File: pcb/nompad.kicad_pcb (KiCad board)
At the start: 2 copper layers, 80.6 x 103.9 mm, 44 parts, among them J1 Conn_01x02_Pin, SW1 ChocHS, SW10 ChocHS, SW11 ChocHS, SW12 ChocHS, SW13 ChocHS, SW14 ChocHS, SW15 ChocHS, SW16 ChocHS, SW17 ChocHS, SW18 ChocHS, SW2 ChocHS, SW3 ChocHS, SW4 ChocHS, SW5 ChocHS, SW6 ChocHS, SW7 ChocHS, SW8 ChocHS, SW9 ChocHS

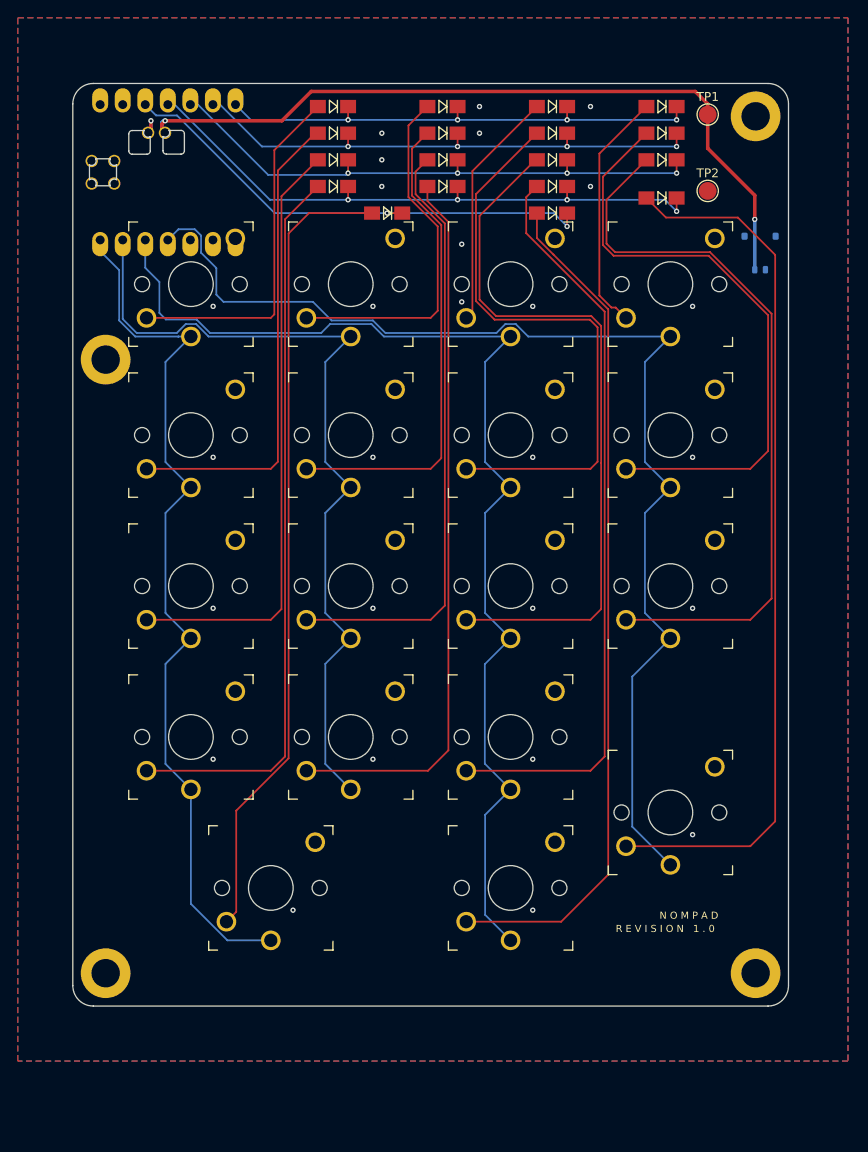
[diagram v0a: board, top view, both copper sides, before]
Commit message: Move one of the screw sockets under case
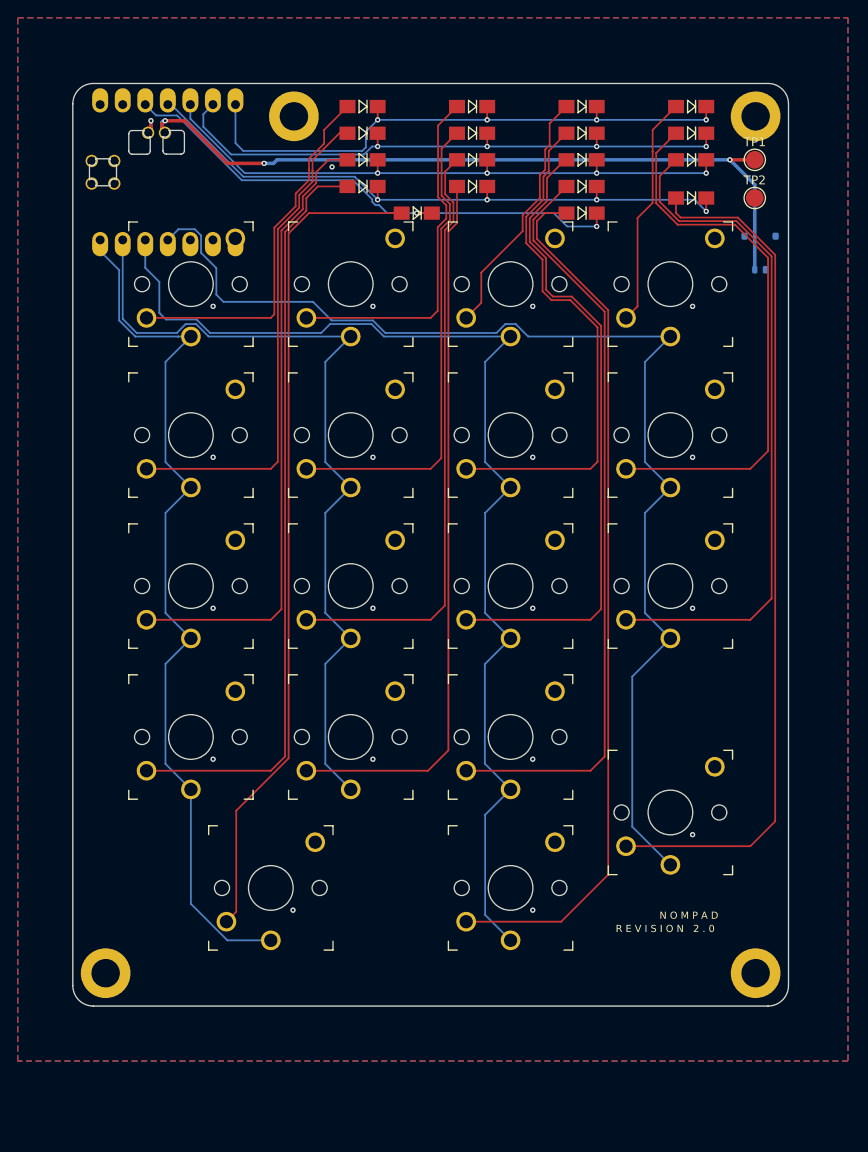
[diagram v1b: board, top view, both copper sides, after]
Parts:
- moved REF** 34.6 mm to (132.6, 49.1)
- moved TP1 7.36 mm to (184.5, 54.0)
- moved TP2 5.36 mm to (184.5, 58.3)
- moved D1 3.33 mm to (140.3, 48.0)
- moved D11 3.33 mm to (165.0, 54.0)
- moved D12 3.33 mm to (177.3, 54.0)
- moved D13 3.33 mm to (140.3, 57.0)
- moved D15 3.33 mm to (165.0, 57.0)
- moved D16 3.33 mm to (177.3, 58.3)
- moved D17 3.33 mm to (146.4, 60.0)
- moved D18 3.33 mm to (165.0, 60.0)
- moved D3 3.33 mm to (165.0, 48.0)
- moved D4 3.33 mm to (177.3, 48.0)
- moved D5 3.33 mm to (140.3, 51.0)
- moved D7 3.33 mm to (165.0, 51.0)
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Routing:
- net /ROW0: track 56.4 -> 66.2 mm
- net Net-(D11-A): track 81.1 -> 72.7 mm
- net Net-(D7-A): track 66.9 -> 58.6 mm
- net /ROW1: track 60.2 -> 68.1 mm
- net Net-(D12-A): track 82.6 -> 76.6 mm
- net Net-(D8-A): track 68.6 -> 62.5 mm
- net /ROW2: track 64.2 -> 68.3 mm
- net /ROW4: track 56.4 -> 59.8 mm
- net /ROW3: track 68.3 -> 71.7 mm
- net Net-(D17-A): track 90.8 -> 94.1 mm
- net Net-(D13-A): track 82.0 -> 85.3 mm
- net Net-(D18-A): track 96.0 -> 98.8 mm
- net Net-(D9-A): track 68.0 -> 70.6 mm
- net Net-(D16-A): track 98.9 -> 96.6 mm
- net BAT: track 86.5 -> 84.6 mm, vias 2 -> 3
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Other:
- board text added: "R E V I S I O N 2 . 0"
- board text removed: "R E V I S I O N 1 . 0"

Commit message: Cleanup
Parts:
- moved TP2 1.84 mm to (185.7, 59.7)
- moved TP1 1.84 mm to (185.7, 55.4)
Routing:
- net /ROW0: track 66.2 -> 68.0 mm
- net BAT: track 84.6 -> 86.4 mm
- net Net-(D11-A): track 72.7 -> 73.4 mm
- net Net-(D15-A): track 85.3 -> 86.0 mm

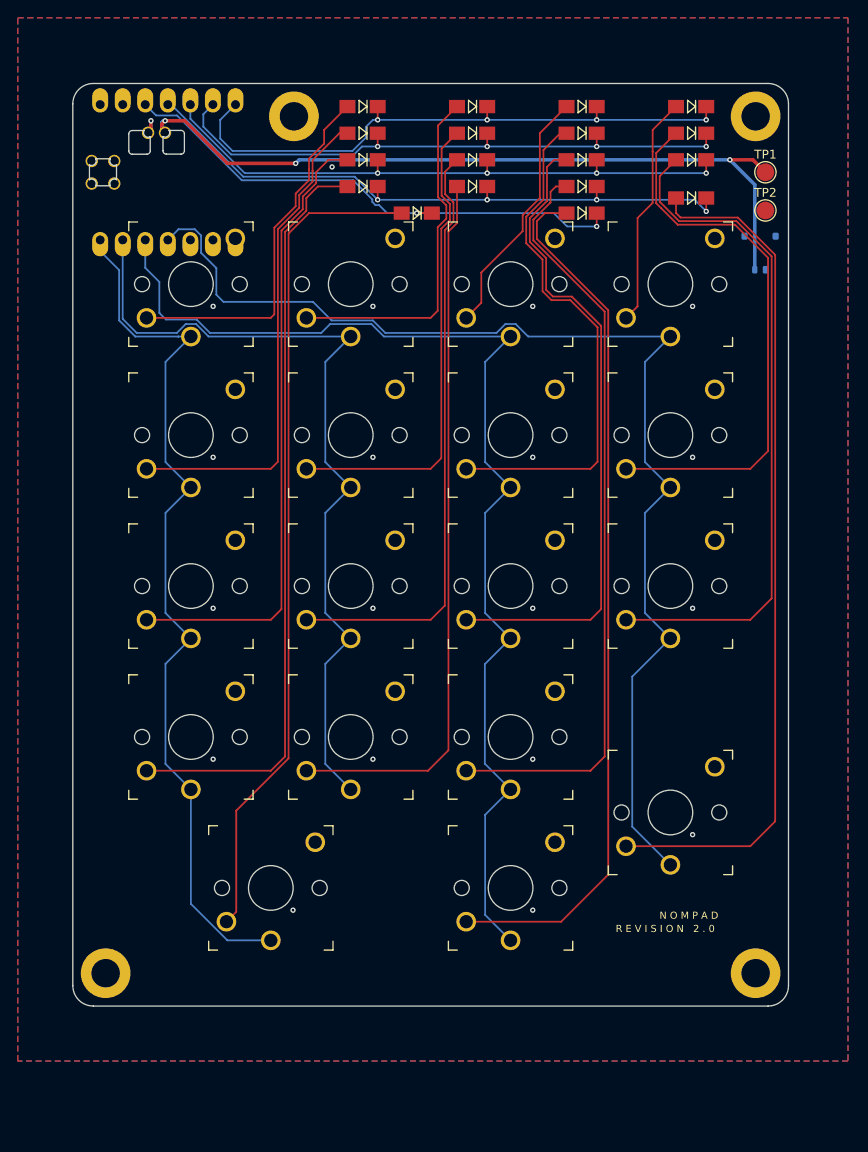
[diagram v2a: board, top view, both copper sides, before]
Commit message: Center everything
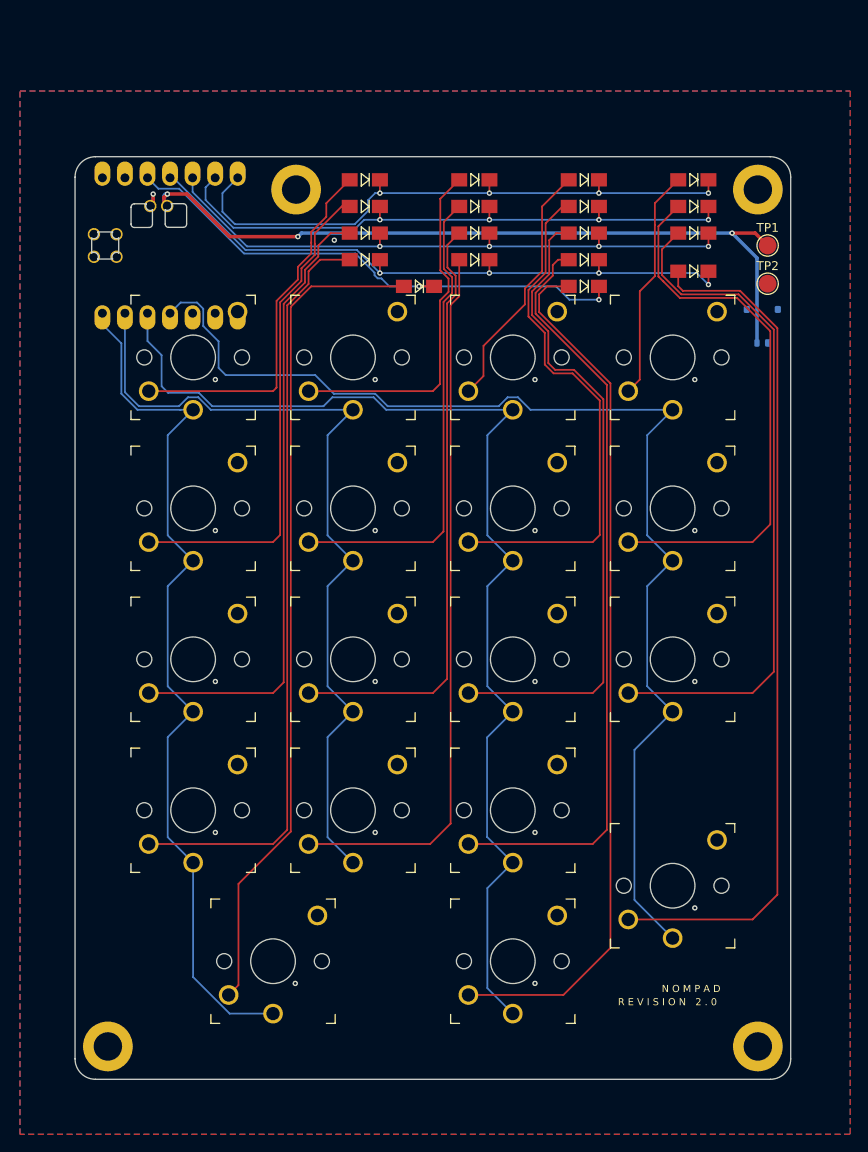
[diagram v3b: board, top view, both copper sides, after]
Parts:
- moved D1 8.25 mm to (140.6, 56.2)
- moved D10 8.25 mm to (152.9, 62.2)
- moved D11 8.25 mm to (165.2, 62.2)
- moved D12 8.25 mm to (177.6, 62.2)
- moved D13 8.25 mm to (140.6, 65.2)
- moved D14 8.25 mm to (152.9, 65.2)
- moved D15 8.25 mm to (165.2, 65.2)
- moved D16 8.25 mm to (177.6, 66.5)
- moved D17 8.25 mm to (146.7, 68.2)
- moved D18 8.25 mm to (165.2, 68.2)
- moved D2 8.25 mm to (152.9, 56.2)
- moved D3 8.25 mm to (165.2, 56.2)
- moved D4 8.25 mm to (177.6, 56.2)
- moved D5 8.25 mm to (140.6, 59.2)
- moved D6 8.25 mm to (152.9, 59.2)
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
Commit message: Align socket
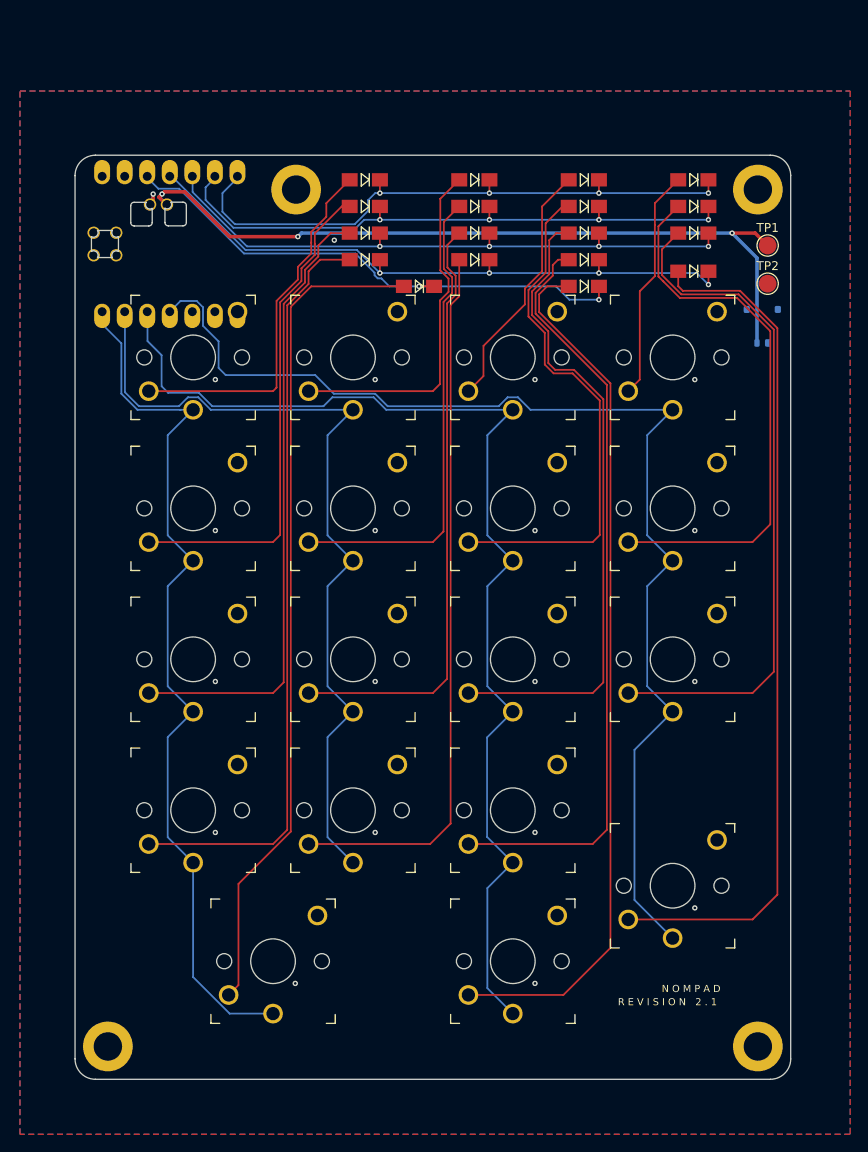
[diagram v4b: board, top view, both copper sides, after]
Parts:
- moved LU1 0.17 mm to (118.6, 63.5)
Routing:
- net BAT: track 86.4 -> 87.2 mm
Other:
- board size 80.6 x 103.9 mm -> 80.6 x 104.1 mm
- board text added: "R E V I S I O N 2 . 1"
- board text removed: "R E V I S I O N 2 . 0"
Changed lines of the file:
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@@
 		(title "Nompad")
 		(date "2025-05-27")
-		(rev "2.0")
+		(rev "2.1")
 	)
 	(layers
@@
 	(footprint "pcb-footprints:xiao-ble-smd-cutout-aternate"
 		(layer "B.Cu")
-		(at 118.65 63.65 -90)
+		(at 118.62 63.48 -90)
 		(property "Reference" "LU1"
 			(at -19.3989 11.28268 90)
@@
 	)
 	(gr_line
-		(start 188.55 55.95)
+		(start 188.55 55.78)
 		(end 188.55 155.25)
 		(stroke
@@
 	)
 	(gr_line
-		(start 107.95 55.95)
+		(start 107.95 55.78)
 		(end 107.95 155.25)
 		(stroke
@@
 	)
 	(gr_arc
-		(start 186.25 53.65)
-		(mid 187.876346 54.323654)
-		(end 188.55 55.95)
+		(start 186.25 53.48)
+		(mid 187.876346 54.153654)
+		(end 188.55 55.78)
 		(stroke
 			(width 0.1)
@@
 	)
 	(gr_line
-		(start 186.25 53.65)
-		(end 110.25 53.65)
+		(start 186.25 53.48)
+		(end 110.25 53.48)
 		(stroke
 			(width 0.1)
@@
 	)
 	(gr_arc
-		(start 107.95 55.95)
-		(mid 108.623654 54.323654)
-		(end 110.25 53.65)
+		(start 107.95 55.78)
+		(mid 108.623654 54.153654)
+		(end 110.25 53.48)
 		(stroke
 			(width 0.1)
@@
 		)
 	)
-	(gr_text "R E V I S I O N   2 . 0"
+	(gr_text "R E V I S I O N   2 . 1"
 		(at 169.083809 148.84 0)
 		(layer "F.SilkS")
@@
 	)
 	(segment
-		(start 181.95 62.25)
-		(end 184.55 62.25)
+		(start 118 57.6)
+		(end 117.75 57.85)
+		(width 0.4)
+		(layer "F.Cu")
+		(net 2)
+	)
+	(segment
+		(start 117.4 58.2)
+		(end 117.949481 58.749481)
 		(width 0.4)
 		(layer "F.Cu")
@@
 	)
 	(segment
-		(start 118.35 57.85)
-		(end 117.971061 58.228939)
+		(start 125.35 62.65)
+		(end 120.3 57.6)
 		(width 0.4)
 		(layer "F.Cu")
@@
 	)
 	(segment
-		(start 117.971061 58.228939)
-		(end 117.971061 58.922401)
+		(start 181.95 62.25)
+		(end 184.55 62.25)
 		(width 0.4)
 		(layer "F.Cu")
@@
 	)
 	(segment
-		(start 120.55 57.85)
-		(end 118.35 57.85)
+		(start 120.3 57.6)
+		(end 118 57.6)
 		(width 0.4)
 		(layer "F.Cu")
@@
 	)
 	(segment
-		(start 125.35 62.65)
-		(end 120.55 57.85)
+		(start 117.75 57.85)
+		(end 117.4 58.2)
 		(width 0.4)
 		(layer "F.Cu")
@@
 	)
 	(via
-		(at 181.95 62.25)
+		(at 117.75 57.85)
 		(size 0.6)
 		(drill 0.3)
@@
 	)
 	(via
-		(at 118.35 57.85)
+		(at 181.95 62.25)
 		(size 0.6)
 		(drill 0.3)
 		(layers "F.Cu" "B.Cu")
-		(free yes)
 		(net 2)
 	)
 	(segment
-		(start 118.009182 58.509182)
-		(end 118.009182 58.909182)
+		(start 117.4 58.2)
+		(end 117.949481 58.749481)
 		(width 0.4)
 		(layer "B.Cu")
@@
 	)
 	(segment
-		(start 118.35 57.85)
-		(end 118.15 57.85)
+		(start 117.75 57.85)
+		(end 117.4 58.2)
 		(width 0.4)
 		(layer "B.Cu")
@@
 	)
 	(segment
-		(start 118.15 57.85)
-		(end 118.009182 57.990818)
-		(width 0.4)
-		(layer "B.Cu")
-		(net 2)
-	)
-	(segment
-		(start 118.009182 57.990818)
-		(end 118.009182 58.509182)
-		(width 0.4)
-		(layer "B.Cu")
-		(net 2)
-	)
-	(segment
 		(start 133.45 62.25)
 		(end 181.95 62.25)
@@
 	)
 	(segment
-		(start 119.851 70.069)
-		(end 118.65 71.27)
-		(width 0.2)
-		(layer "B.Cu")
-		(net 14)
-	)
-	(segment
 		(start 159.239799 82.15)
 		(end 157.832799 80.743)
@@
 	)
 	(segment
-		(start 122.391 72.71747)
-		(end 122.391 70.77253)
-		(width 0.2)
-		(layer "B.Cu")
-		(net 14)
-	)
-	(segment
 		(start 143.157301 81.749)
 		(end 141.750301 80.342)
@@
 	)
 	(segment
-		(start 124.1155 74.44197)
-		(end 122.391 72.71747)
-		(width 0.2)
-		(layer "B.Cu")
-		(net 14)
-	)
-	(segment
-		(start 122.391 70.77253)
-		(end 121.68747 70.069)
+		(start 122.361 72.68747)
+		(end 122.361 70.60253)
 		(width 0.2)
 		(layer "B.Cu")
@@
 	)
 	(segment
-		(start 121.68747 70.069)
-		(end 119.851 70.069)
+		(start 119.821 69.899)
+		(end 118.62 71.1)
+		(width 0.2)
+		(layer "B.Cu")
+		(net 14)
+	)
+	(segment
+		(start 124.1155 74.44197)
+		(end 122.361 72.68747)
 		(width 0.2)
 		(layer "B.Cu")
@@
 	)
 	(segment
+		(start 122.361 70.60253)
+		(end 121.65747 69.899)
+		(width 0.2)
+		(layer "B.Cu")
+		(net 14)
+	)
+	(segment
 		(start 172.3845 96.2845)
 		(end 172.3845 85.0155)
@@
 	)
 	(segment
+		(start 121.65747 69.899)
+		(end 119.821 69.899)
+		(width 0.2)
+		(layer "B.Cu")
+		(net 14)
+	)
+	(segment
 		(start 166.95 68.25)
 		(end 166.95 69.683333)
@@
 		(net 0)
 		(net_name "")
-		(locked yes)
 		(layers "F.Cu" "B.Cu")
 		(hatch full 0.5)

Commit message: Shrink PCB
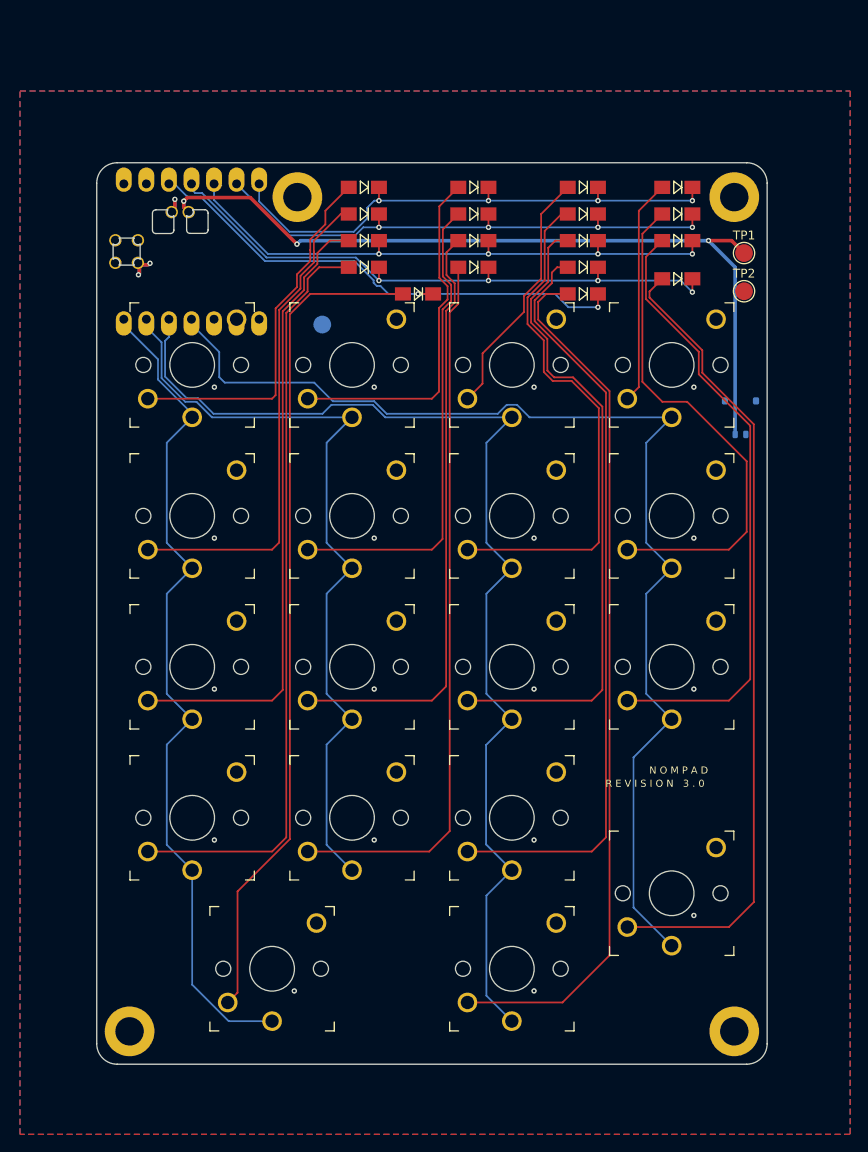
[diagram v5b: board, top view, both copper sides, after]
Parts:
- added ?: , , B.Cu at (135.8, 72.5)
- moved J1 10.6 mm to (182.9, 83.0)
- moved REF** 3.15 mm to (182.2, 152.2)
- moved REF** 2.98 mm to (114.1, 152.2)
- moved REF** 2.79 mm to (182.2, 58.2)
- moved TP1 2.79 mm to (183.3, 64.5)
- moved TP2 2.79 mm to (183.3, 68.8)
- moved LU1 2.59 mm to (121.1, 64.3)
- moved D16 2.00 mm to (175.8, 67.4)
- moved D12 2.00 mm to (175.8, 63.1)
- moved D4 2.00 mm to (175.8, 57.1)
- moved D8 2.00 mm to (175.8, 60.1)
- moved REF** 0.86 mm to (133.0, 58.2)
- moved D1 0.86 mm to (140.5, 57.1)
- moved D5 0.86 mm to (140.5, 60.1)
- moved D9 0.86 mm to (140.5, 63.1)
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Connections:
- LU1 pad 1: (no net) -> unconnected-(LU1-P0.02/0-Pad1)
- LU1 pad 10: (no net) -> unconnected-(LU1-3V3-Pad10)
- LU1 pad 2: (no net) -> unconnected-(LU1-P0.03/1-Pad2)
- LU1 pad 8: (no net) -> unconnected-(LU1-5V-Pad8)
- LU1 pad 9: GND -> unconnected-(LU1-GND-Pad9)
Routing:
- net /ROW1: track 68.1 -> 60.1 mm
- net /ROW0: track 68.0 -> 60.4 mm
- net Net-(D12-A): track 76.6 -> 69.9 mm
- net /COL1: track 94.4 -> 88.7 mm
- net Net-(D16-A): track 96.6 -> 91.1 mm
- net Net-(D8-A): track 62.5 -> 57.5 mm
- net GND: track 2.27 -> 7.06 mm, vias 20 -> 21
- net /COL0: track 100.5 -> 96.0 mm
- net /COL3: track 133.8 -> 129.3 mm
- net BAT: track 87.2 -> 91.3 mm
- net /ROW3: track 71.7 -> 67.9 mm
- net /ROW2: track 68.3 -> 65.0 mm
- net /ROW4: track 59.8 -> 57.8 mm
- net /COL2: track 127.9 -> 125.9 mm
- net Net-(D4-A): track 27.1 -> 26.1 mm
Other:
- board size 80.6 x 104.1 mm -> 75.5 x 101.5 mm
- board text added: "R E V I S I O N 3 . 0"
- board text removed: "R E V I S I O N 2 . 1"
